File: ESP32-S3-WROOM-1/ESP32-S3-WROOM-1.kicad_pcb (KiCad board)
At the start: 2 copper layers, 25.4 x 57 mm, 23 parts, among them J1 ESP32-S3-DEVKITC-1-J1, J2 ESP32-S3-DEVKITC-1-J2, J3 UART, P1 USB2.0_C_12pin, SW1 EN, SW2 BOOT, U1 ESP32-S3-WROOM-1, U2 AMS1117-3.3

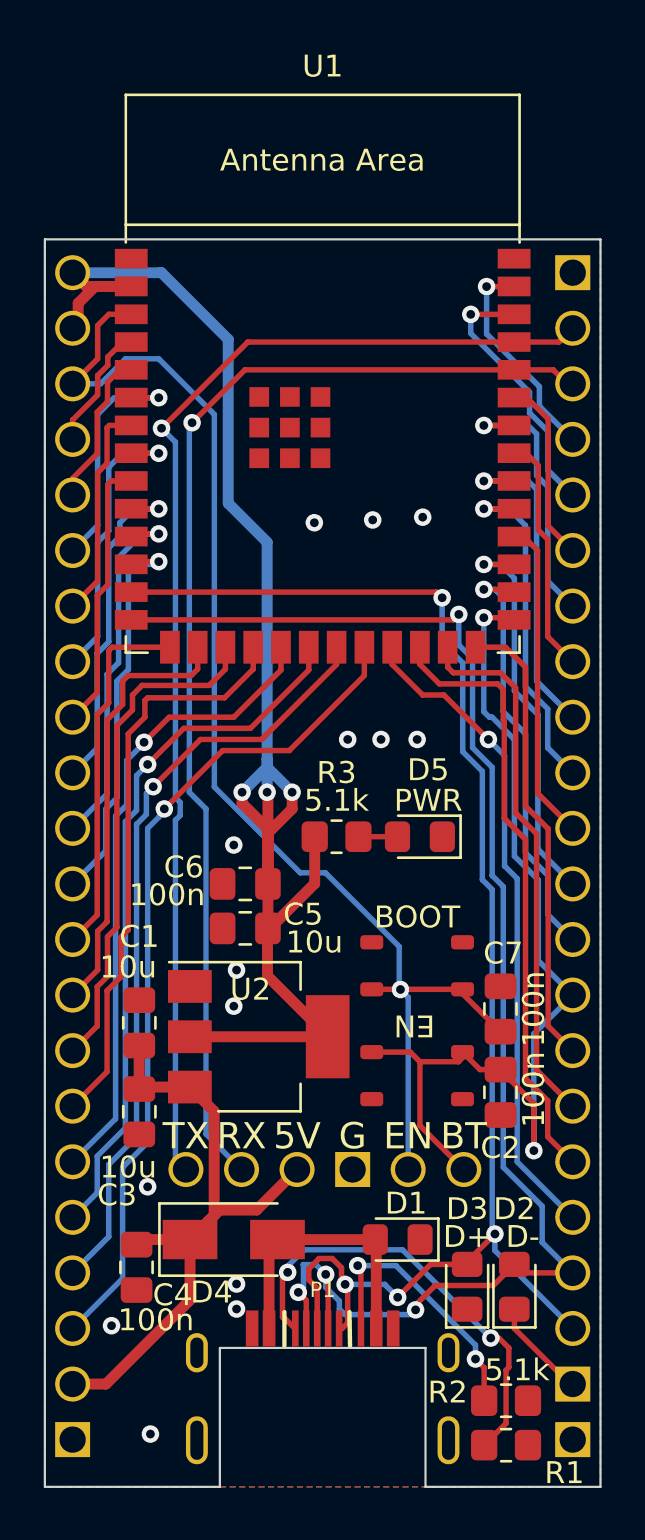
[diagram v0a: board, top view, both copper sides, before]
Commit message: update SILK
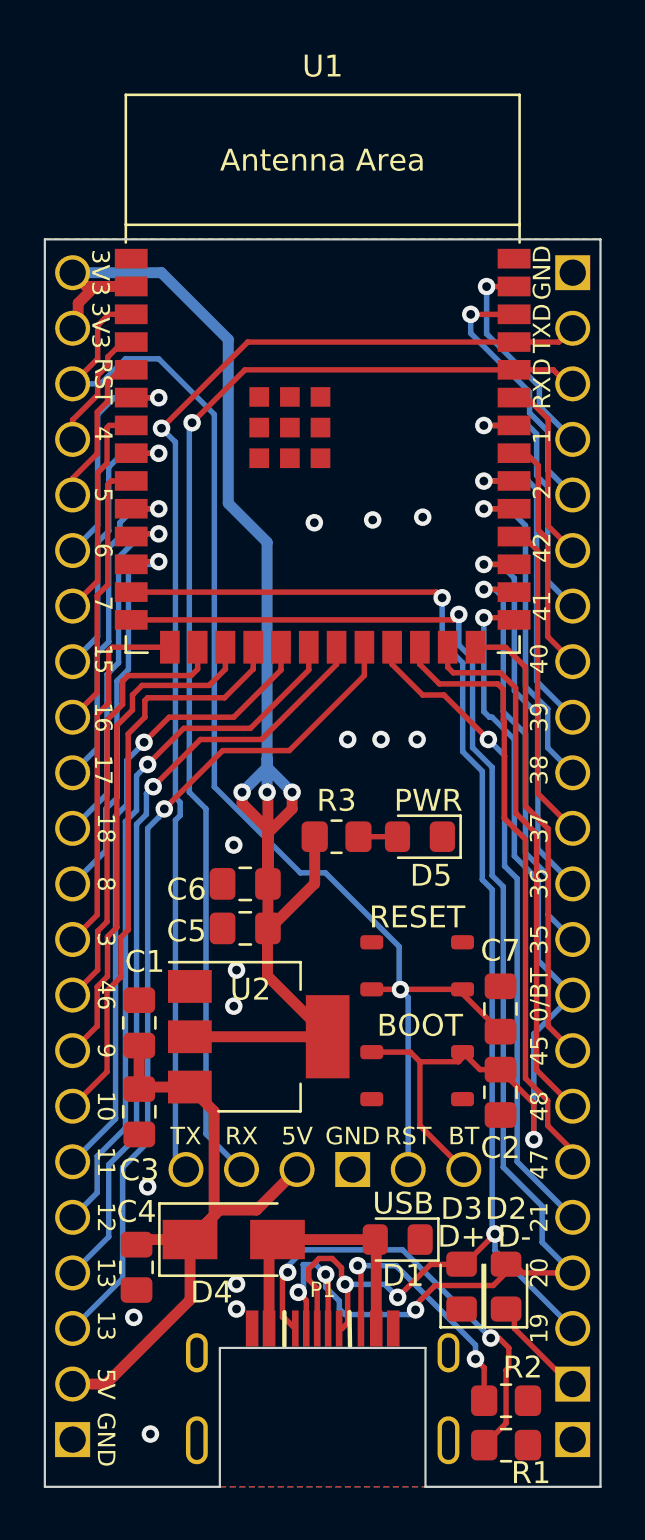
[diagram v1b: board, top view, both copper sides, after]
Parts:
- D1: value LED -> USB
- SW1: value EN -> BOOT
- SW2: value BOOT -> RESET
- moved D2 0.38 mm to (85.9, 84.4)
- moved D3 0.25 mm to (83.8, 84.4)
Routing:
- net GPIO0: track 45.0 -> 43.9 mm
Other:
- board text added: "0/BT"
- board text added: "1"
- board text added: "10"
- board text added: "11"
- board text added: "12"
- board text added: "13"
- board text added: "15"
- board text added: "16"
- board text added: "17"
- board text added: "18"
- board text added: "19"
- board text added: "2"
- board text added: "20"
- board text added: "21"
- board text added: "3"
- board text added: "35"
- board text added: "36"
- board text added: "37"
- board text added: "38"
- board text added: "39"
- board text added: "3V3"
- board text added: "4"
- board text added: "40"
- board text added: "41"
- board text added: "42"
- board text added: "45"
- board text added: "46"
- board text added: "47"
- board text added: "48"
- board text added: "5"
- board text added: "5V"
- board text added: "6"
- board text added: "7"
- board text added: "8"
- board text added: "9"
- board text added: "GND"
- board text added: "RST"
- board text added: "RXD"
- board text added: "TXD"

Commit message: 漏れ
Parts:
- removed C7: 100n, Capacitor_SMD:C_0805_2012Metric_Pad1.18x1.45mm_HandSolder
- added R4: 10k, Resistor_SMD:R_0805_2012Metric_Pad1.20x1.40mm_HandSolder, F.Cu at (78.2, 60.3)
- D1: value USB -> 5V
- moved C2 15.6 mm to (82.0, 60.3), turned to 0 degrees
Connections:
- C2 pad 1: GPIO0 -> CHIP_PU
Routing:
- net CHIP_PU: track 58.6 -> 63.8 mm, vias 1 -> 2
- net +3V3: track 72.5 -> 76.1 mm

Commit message: 漏れ
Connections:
- net VBUS renamed Net-(D1-Pad2)
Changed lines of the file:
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@@
   (net 4 "+3V3")
   (net 5 "CHIP_PU")
-  (net 6 "VBUS")
+  (net 6 "Net-(D1-Pad2)")
   (net 7 "GPIO20")
   (net 8 "GPIO19")
@@
       (net 1 "+5V") (pinfunction "K") (pintype "passive"))
     (pad "2" smd rect (at 2 0) (size 2.5 1.8) (layers "F.Cu" "F.Paste" "F.Mask")
-      (net 6 "VBUS") (pinfunction "A") (pintype "passive"))
+      (net 6 "Net-(D1-Pad2)") (pinfunction "A") (pintype "passive"))
     (model "${KICAD6_3DMODEL_DIR}/Diode_SMD.3dshapes/D_SMA.wrl"
       (offset (xyz 0 0 0))
@@
       (net 2 "GND") (pinfunction "GND_A1/B12") (pintype "power_out") (zone_connect 2))
     (pad "2" smd rect (at -2.45 0 180) (size 0.575 1.65) (layers "F.Cu" "F.Paste" "F.Mask")
-      (net 6 "VBUS") (pinfunction "VBUS_A4/B9") (pintype "power_out"))
+      (net 6 "Net-(D1-Pad2)") (pinfunction "VBUS_A4/B9") (pintype "power_out"))
     (pad "4" smd rect (at -1.25 0 180) (size 0.3 1.65) (layers "F.Cu" "F.Paste" "F.Mask")
       (net 43 "Net-(P1-Pad4)") (pinfunction "CC1_A5") (pintype "passive"))
@@
       (net 44 "Net-(P1-Pad10)") (pinfunction "CC2_B5") (pintype "passive"))
     (pad "11" smd rect (at 2.45 0 180) (size 0.575 1.65) (layers "F.Cu" "F.Paste" "F.Mask")
-      (net 6 "VBUS") (pinfunction "VBUS_B4/A9") (pintype "power_out"))
+      (net 6 "Net-(D1-Pad2)") (pinfunction "VBUS_B4/A9") (pintype "power_out"))
     (pad "12" smd rect (at 3.225 0 180) (size 0.575 1.65) (layers "F.Cu" "F.Paste" "F.Mask")
       (net 2 "GND") (pinfunction "GND_A12/B1") (pintype "power_out") (zone_connect 2))
@@
       (net 2 "GND") (pinfunction "K") (pintype "passive") (zone_connect 2))
     (pad "2" smd roundrect (at 1.025 0 180) (size 1.15 1.4) (layers "F.Cu" "F.Paste" "F.Mask") (roundrect_rratio 0.217391)
-      (net 6 "VBUS") (pinfunction "A") (pintype "passive"))
+      (net 6 "Net-(D1-Pad2)") (pinfunction "A") (pintype "passive"))
     (model "${KICAD6_3DMODEL_DIR}/LED_SMD.3dshapes/LED_0805_2012Metric.wrl"
       (offset (xyz 0 0 0))
